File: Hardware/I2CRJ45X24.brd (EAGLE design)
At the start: 216 x 50 mm, 129 parts, among them IC1 MCP23017SO, IC2 MCP23017SO, IC3 MCP23017SO, IC4 MCP23017SO, IC5 MCP23017SO, IC6 MCP23017SO, J1 I2C-BREAKOUT, J2 I2C-BREAKOUT, J3 M01-PLAIN, J4 RJ45-X8, J5 RJ45-X8, J6 RJ45-X8

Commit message: Major rework for v3.0 release of all versions.
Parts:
- R101: value 22K -> 10K
- SJ3: device SuperHouse-Jumpers:SJC -> SuperHouse-Jumpers:SJ
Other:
- board text added: "24-Port I2C RJ45 Breakout"
- board text removed: "24-Channel I2C RJ45 Breakout"
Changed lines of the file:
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@@
 </layers>
 <board>
-<fusionsync huburn="a.cGVyc29uYWw6dWUyZDliZmNi" projecturn="a.cGVyc29uYWw6dWUyZDliZmNiIzIwMTkwNjE5MTk5NjgzNjgx" f3durn="urn:adsk.wipprod:dm.lineage:7PE12rU6Rs2d8xNWJ3I8mw" pcbguid="240f1cde-c83f-4e3e-9fac-562d2bf45fdf" lastpulledtime="" lastsyncedchangeguid="1491f9b9-a179-9c0a-9821-19275fe4b9b0" latestrevisionid="" lastsyncedrevisionid="" lastboardhashguid="57911f44-b240-5674-ec1f-8acbffdfcb08" lastpushedtime="2021-04-15T04:03:47Z" linktopcb3d="false"/>
+<fusionsync huburn="a.cGVyc29uYWw6dWUyZDliZmNi" projecturn="a.cGVyc29uYWw6dWUyZDliZmNiIzIwMTkwNjE5MTk5NjgzNjgx" f3durn="urn:adsk.wipprod:dm.lineage:7PE12rU6Rs2d8xNWJ3I8mw" pcbguid="240f1cde-c83f-4e3e-9fac-562d2bf45fdf" lastpulledtime="" lastsyncedchangeguid="1491f9b9-a179-9c0a-9821-19275fe4b9b0" latestrevisionid="" lastsyncedrevisionid="" lastboardhashguid="93750741-3b2d-7ddd-64bd-c7f7c55b0702" lastpushedtime="2021-04-15T05:51:18Z" linktopcb3d="false"/>
 <plain>
 <wire x1="3" y1="0" x2="0" y2="3" width="0" layer="20" curve="-90"/>
@@
 <text x="50.045" y="43.854" size="3.1" layer="22" font="vector" ratio="17" distance="30" rot="MR0" align="center-left">Super
 House</text>
-<text x="60.045" y="27" size="2.8" layer="22" font="vector" ratio="17" distance="20" rot="MR0">24-Channel
+<text x="60.045" y="27" size="2.8" layer="22" font="vector" ratio="17" distance="20" rot="MR0">24-Port
 I2C RJ45
 Breakout</text>
@@
 <text x="4.5" y="12" size="1.6" layer="21" font="vector" ratio="17" distance="20" align="bottom-center">Super
 House</text>
-<text x="12" y="47.354" size="1.8" layer="21" font="vector" ratio="17" distance="30">24-Channel I2C RJ45 Breakout</text>
+<text x="11" y="47.354" size="2.1844" layer="21" font="vector" ratio="17" distance="30">24-Port I2C RJ45 Breakout</text>
 <text x="32" y="45.354" size="1.6764" layer="21" font="vector" ratio="17" distance="30">by Jon Oxer</text>
 <text x="40.5" y="24.955" size="1.9304" layer="21" font="vector" ratio="17" rot="R90">VCC: 1.8-5.5V
@@
 <attribute name="VALUE" x="122.484" y="46.603" size="0.4064" layer="27"/>
 </element>
-<element name="SJ2" library="SuperHouse-Jumpers" library_urn="urn:adsk.eagle:library:12190622" package="SJ" package3d_urn="urn:adsk.eagle:package:7066338/1" value="SCL PU" x="64.5" y="46" smashed="yes" rot="R90">
+<element name="SJ2" library="SuperHouse-Jumpers" library_urn="urn:adsk.eagle:library:12190622" package="SJ" package3d_urn="urn:adsk.eagle:package:7066338/2" value="SCL PU" x="64.5" y="46" smashed="yes" rot="R90">
 <attribute name="NAME" x="63.357" y="44.349" size="1.27" layer="25" ratio="10" rot="R90"/>
 <attribute name="VALUE" x="64.5" y="46.4001" size="0.02" layer="27" rot="R90"/>
 </element>
-<element name="SJ1" library="SuperHouse-Jumpers" library_urn="urn:adsk.eagle:library:12190622" package="SJ" package3d_urn="urn:adsk.eagle:package:7066338/1" value="SDA PU" x="61.5" y="46" smashed="yes" rot="R90">
+<element name="SJ1" library="SuperHouse-Jumpers" library_urn="urn:adsk.eagle:library:12190622" package="SJ" package3d_urn="urn:adsk.eagle:package:7066338/2" value="SDA PU" x="61.5" y="46" smashed="yes" rot="R90">
 <attribute name="NAME" x="60.357" y="44.349" size="1.27" layer="25" ratio="10" rot="R90"/>
 <attribute name="VALUE" x="61.5" y="46.4001" size="0.02" layer="27" rot="R90"/>
@@
 <attribute name="VALUE" x="214.9652" y="20.984" size="0.4064" layer="27" font="vector" rot="R90"/>
 </element>
-<element name="R101" library="SuperHouse-DiscreteSemi" library_urn="urn:adsk.eagle:library:11768461" package="R0603" package3d_urn="urn:adsk.eagle:package:11768543/2" value="22K" x="3.6" y="23.1" smashed="yes" rot="R180">
+<element name="R101" library="SuperHouse-DiscreteSemi" library_urn="urn:adsk.eagle:library:11768461" package="R0603" package3d_urn="urn:adsk.eagle:package:11768543/2" value="10K" x="3.6" y="23.1" smashed="yes" rot="R180">
 <attribute name="NAME" x="4.489" y="22.592" size="0.4064" layer="25" font="vector" rot="R180"/>
 <attribute name="VALUE" x="4.616" y="24.0652" size="0.4064" layer="27" font="vector" rot="R180"/>
 </element>
-<element name="SJ3" library="SuperHouse-Jumpers" library_urn="urn:adsk.eagle:library:12190622" package="SJC" package3d_urn="urn:adsk.eagle:package:7066342/2" value="RST-PU" x="8.4" y="46.9" smashed="yes" rot="R270">
+<element name="SJ3" library="SuperHouse-Jumpers" library_urn="urn:adsk.eagle:library:12190622" package="SJ" package3d_urn="urn:adsk.eagle:package:7066338/2" value="RST-PU" x="8.4" y="46.9" smashed="yes" rot="R270">
 <attribute name="NAME" x="9.543" y="48.551" size="1.27" layer="25" ratio="10" rot="R270"/>
 <attribute name="VALUE" x="8.4" y="46.4999" size="0.02" layer="27" rot="R270"/>
@@
 <wire x1="115.62" y1="42.62" x2="115" y2="42" width="0.4064" layer="1"/>
 <wire x1="83" y1="42" x2="82.9" y2="41.9" width="0.3048" layer="1"/>
-<wire x1="82.9" y1="41.9" x2="70" y2="41.9" width="0.3048" layer="1"/>
-<wire x1="70" y1="41.9" x2="62.9" y2="41.9" width="0.3048" layer="1"/>
-<wire x1="62.9" y1="41.9" x2="62" y2="41" width="0.3048" layer="1"/>
-<wire x1="62" y1="41" x2="62" y2="40" width="0.3048" layer="1"/>
-<wire x1="62" y1="40" x2="59.54" y2="37.54" width="0.3048" layer="1"/>
-<wire x1="59.54" y1="37.54" x2="58.78" y2="37.54" width="0.3048" layer="1"/>
+<wire x1="82.9" y1="41.9" x2="70" y2="41.9" width="0.4064" layer="1"/>
+<wire x1="70" y1="41.9" x2="62.9" y2="41.9" width="0.4064" layer="1"/>
+<wire x1="62.9" y1="41.9" x2="62" y2="41" width="0.4064" layer="1"/>
+<wire x1="62" y1="41" x2="62" y2="40" width="0.4064" layer="1"/>
+<wire x1="62" y1="40" x2="59.54" y2="37.54" width="0.4064" layer="1"/>
+<wire x1="59.54" y1="37.54" x2="58.78" y2="37.54" width="0.4064" layer="1"/>
 <wire x1="64.5" y1="46.762" x2="61.5" y2="46.762" width="0.3048" layer="1"/>
 <wire x1="61.5" y1="46.762" x2="60.238" y2="46.762" width="0.3048" layer="1"/>

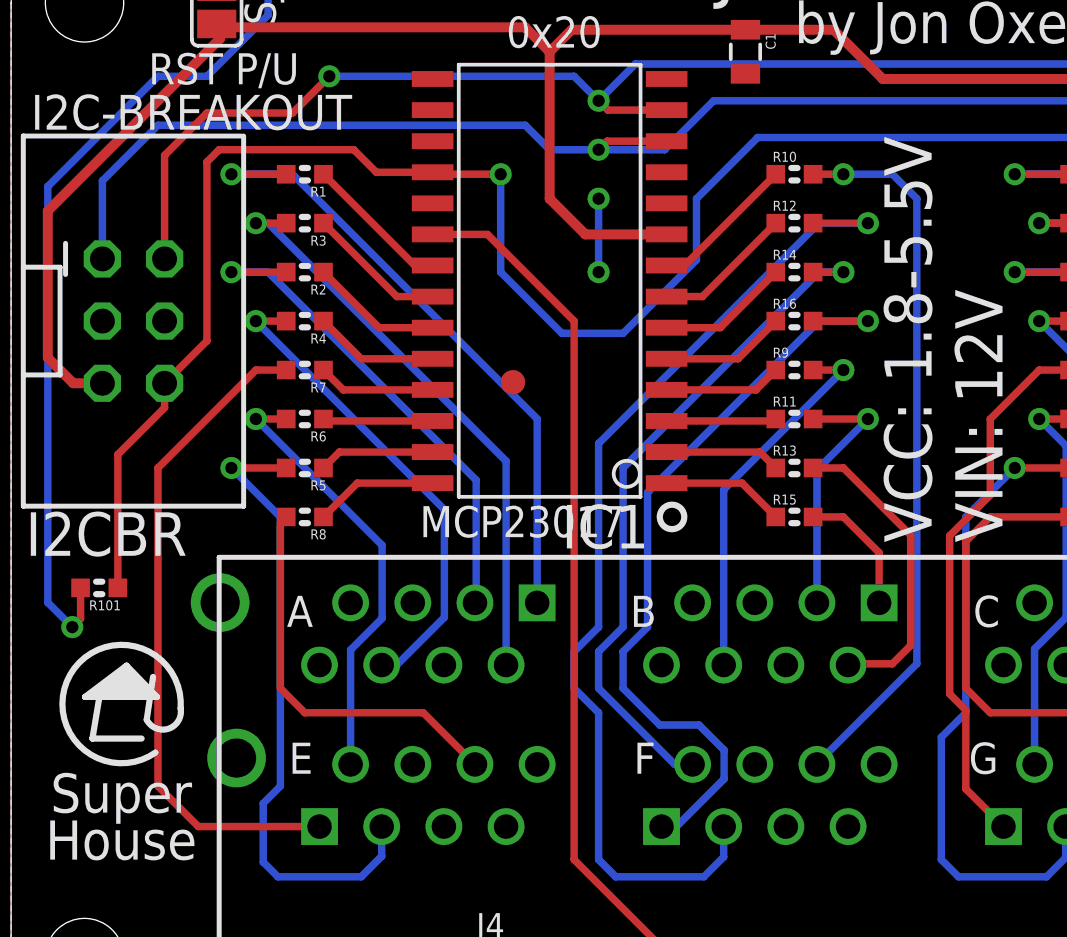
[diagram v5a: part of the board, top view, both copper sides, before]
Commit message: Began replacement of discrete resistors with resistor arrays.
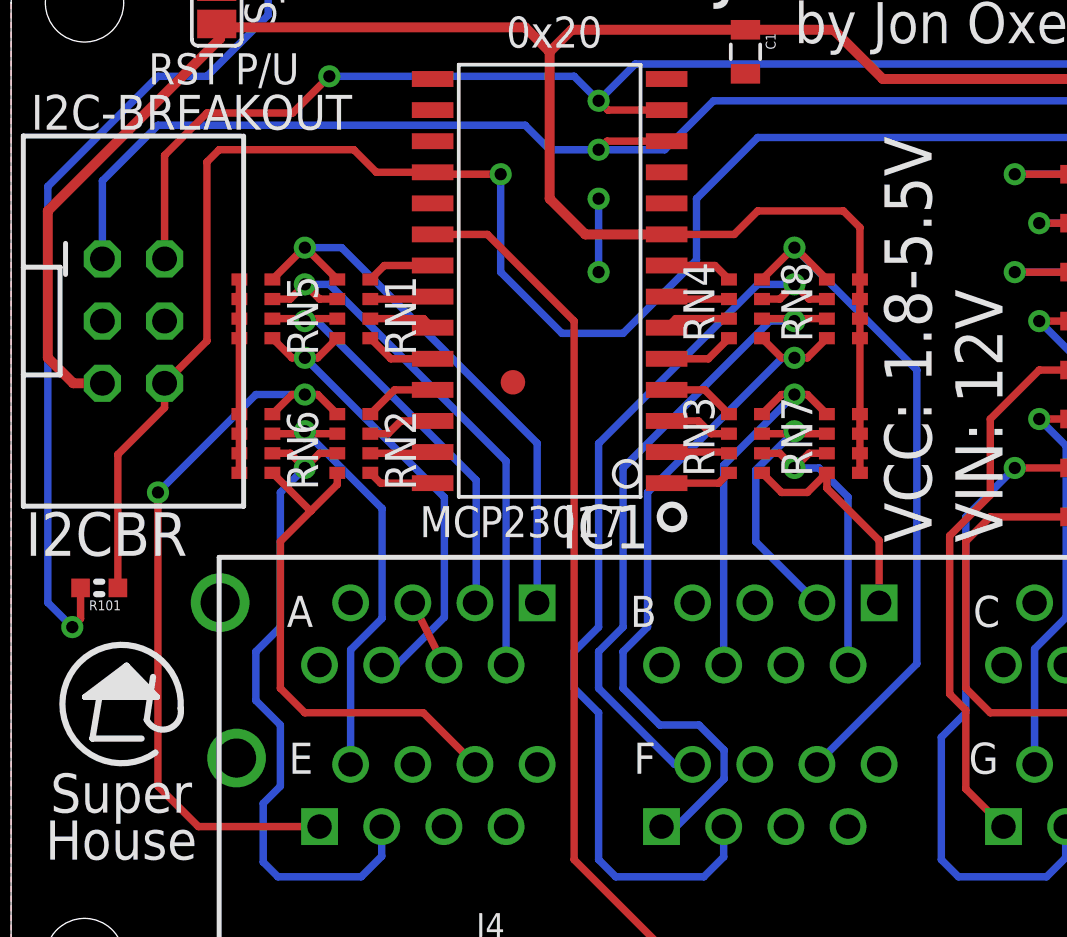
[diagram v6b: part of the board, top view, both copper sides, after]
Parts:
- removed R1, R10, R11, R12, R13, R14, R15, R16, R2, R3, R4, R5, R6, R7, R8, R9: 1K, SuperHouse-DiscreteSemi:R0603
- added RN1, RN2, RN3, RN4: 1K, SuperHouse-DiscreteSemi:CAY16
- added RN5, RN6, RN7, RN8: (no value), SuperHouse-DiscreteSemi:CAY16
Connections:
- net 1A1: now also RN1.5, RN5.4; no longer R1.2
- net 1A2: now also RN1.6, RN5.3; no longer R3.2
- net 1A3: now also RN1.7, RN5.2; no longer R2.2
- net 1A6: now also RN1.8, RN5.1; no longer R4.2
- net 1B1: now also RN3.5, RN7.4; no longer R15.2
- net 1B2: now also RN3.6, RN7.3; no longer R13.2
- net 1B3: now also RN3.7, RN7.2; no longer R11.2
- net 1B6: now also RN3.8, RN7.1; no longer R9.2
- net 1E1: now also RN2.5, RN6.4; no longer R7.2
- net 1E2: now also RN2.6, RN6.3; no longer R6.2
- net 1E3: now also RN2.7, RN6.2; no longer R5.2
- net 1E6: now also RN2.8, RN6.1; no longer R8.2
- net 1F1: now also RN4.5, RN8.4; no longer R16.2
- net 1F2: now also RN4.6, RN8.3; no longer R14.2
- net 1F3: now also RN4.7, RN8.2; no longer R12.2
- net 1F6: now also RN4.8, RN8.1; no longer R10.2
- net GPA0-1: now also RN1.4; no longer R1.1
- net GPA1-1: now also RN1.3; no longer R3.1
- net GPA2-1: now also RN1.2; no longer R2.1
- net GPA3-1: now also RN1.1; no longer R4.1
- net GPA4-1: now also RN2.4; no longer R7.1
- net GPA5-1: now also RN2.3; no longer R6.1
- net GPA6-1: now also RN2.2; no longer R5.1
- net GPA7-1: now also RN2.1; no longer R8.1
- net GPB0-1: now also RN3.4; no longer R15.1
- net GPB1-1: now also RN3.3; no longer R13.1
- net GPB2-1: now also RN3.2; no longer R11.1
- net GPB3-1: now also RN3.1; no longer R9.1
- net GPB4-1: now also RN4.4; no longer R16.1
- net GPB5-1: now also RN4.3; no longer R14.1
- net GPB6-1: now also RN4.2; no longer R12.1
- net GPB7-1: now also RN4.1; no longer R10.1
- net VCC: now also RN5.5, RN5.6, RN5.7, RN5.8, RN6.5, RN6.6, RN6.7, RN6.8, RN7.5, RN7.6, RN7.7, RN7.8, RN8.5, RN8.6, RN8.7, RN8.8
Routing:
- net VCC: track 327.1 -> 353.6 mm
- net 1E6: track 16.3 -> 21.2 mm
- net 1B1: track 5.35 -> 9.51 mm
- net 1A1: track 26.4 -> 23.0 mm
- net 1A3: track 20.8 -> 17.5 mm
- net GPB7-1: track 6.00 -> 2.78 mm
- net GPA0-1: track 6.00 -> 2.78 mm
- net 1F3: track 41.8 -> 38.6 mm
- net GPB6-1: track 5.70 -> 2.59 mm
- net GPA1-1: track 5.70 -> 2.59 mm
- net 1E1: track 27.2 -> 30.3 mm, vias 0 -> 2
- net VIN: track 16.7 -> 19.6 mm
- net GPB5-1: track 5.40 -> 2.70 mm
- net GPA2-1: track 5.40 -> 2.70 mm
- net 1F1: track 32.3 -> 29.7 mm
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
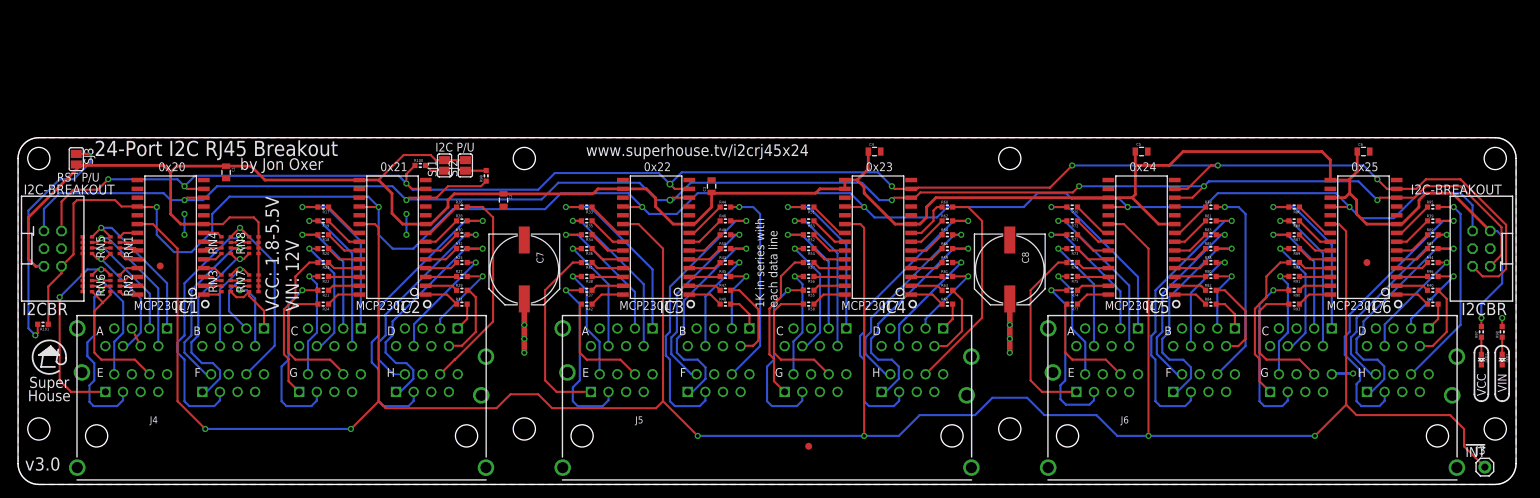
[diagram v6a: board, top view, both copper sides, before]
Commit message: Progress on converting resistors to arrays and adding pullups.
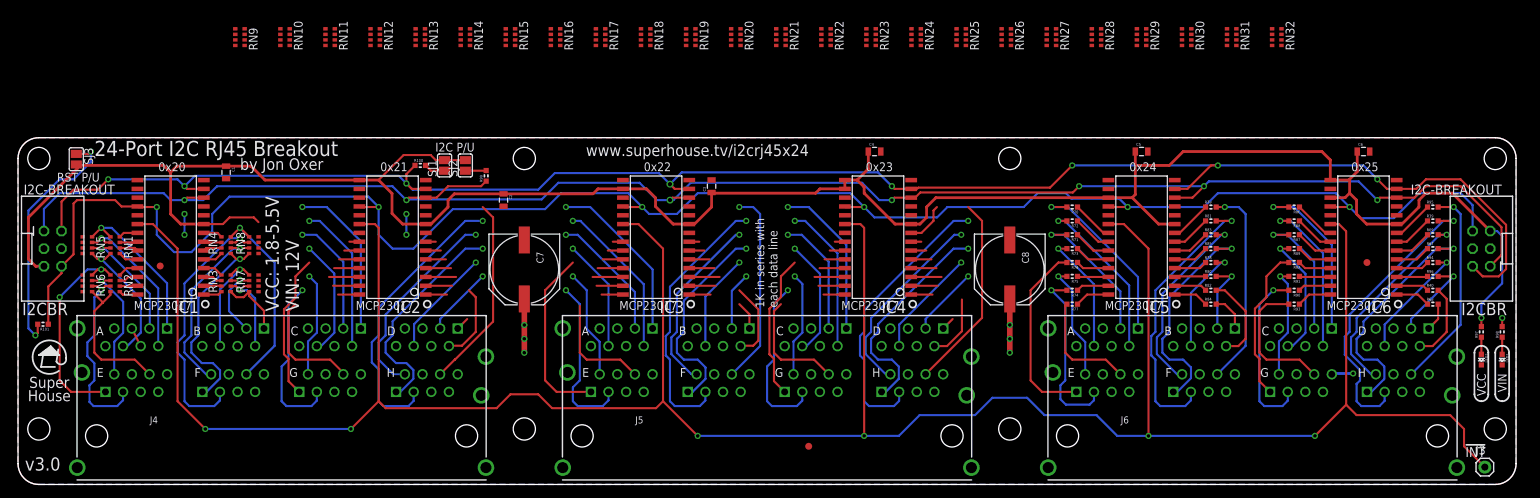
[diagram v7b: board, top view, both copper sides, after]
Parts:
- removed R17, R18, R19, R20, R21, R22, R23, R24, R25, R26, R27, R28, R29, R30, R31, R32, R33, R34, R35, R36, R37, R38, R41, R42, R43, R44, R45, R46, R47, R48, R49, R50, R51, R52, R53, R54, R55, R56, R57, R58, R59, R60, R61, R62, R63, R64, R65, R66: 1K, SuperHouse-DiscreteSemi:R0603
- added RN10, RN11, RN12, RN17, RN18, RN19, RN20, RN25, RN26, RN27, RN28, RN9: 1K, SuperHouse-DiscreteSemi:CAY16
- added RN13, RN14, RN15, RN16, RN21, RN22, RN23, RN24, RN29, RN30, RN31, RN32: 10K, SuperHouse-DiscreteSemi:CAY16
- RN5, RN6, RN7, RN8: value (none) -> 10K
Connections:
- net 1C1: now also RN13.4, RN9.5; no longer R17.2
- net 1C2: now also RN13.3, RN9.6; no longer R19.2
- net 1C3: now also RN13.2, RN9.7; no longer R18.2
- net 1C6: now also RN13.1, RN9.8; no longer R20.2
- net 1D1: now also RN11.5, RN15.4; no longer R31.2
- net 1D2: now also RN11.6, RN15.3; no longer R29.2
- net 1D3: now also RN11.7, RN15.2; no longer R27.2
- net 1D6: now also RN11.8, RN15.1; no longer R25.2
- net 1G1: now also RN10.5, RN14.4; no longer R23.2
- net 1G2: now also RN10.6, RN14.3; no longer R22.2
- net 1G3: now also RN10.7, RN14.2; no longer R21.2
- net 1G6: now also RN10.8, RN14.1; no longer R24.2
- net 1H1: now also RN12.5, RN16.4; no longer R32.2
- net 1H2: now also RN12.6, RN16.3; no longer R30.2
- net 1H3: now also RN12.7, RN16.2; no longer R28.2
- net 1H6: now also RN12.8, RN16.1; no longer R26.2
- net 2A1: now also RN17.5, RN21.4; no longer R33.2
- net 2A2: now also RN17.6, RN21.3; no longer R35.2
- net 2A3: now also RN17.7, RN21.2; no longer R34.2
- net 2A6: now also RN17.8, RN21.1; no longer R36.2
- net 2B1: now also RN19.5, RN23.4; no longer R49.2
- net 2B2: now also RN19.6, RN23.3; no longer R47.2
- net 2B3: now also RN19.7, RN23.2; no longer R45.2
- net 2B6: now also RN19.8, RN23.1; no longer R43.2
- net 2C1: now also RN25.5, RN29.4; no longer R51.2
- net 2C2: now also RN25.6, RN29.3; no longer R53.2
- net 2C3: now also RN25.7, RN29.2; no longer R52.2
- net 2C6: now also RN25.8, RN29.1; no longer R54.2
- net 2D1: now also RN27.5, RN31.4; no longer R65.2
- net 2D2: now also RN27.6, RN31.3; no longer R63.2
- net 2D3: now also RN27.7, RN31.2; no longer R61.2
- net 2D6: now also RN27.8, RN31.1; no longer R59.2
- net 2E1: now also RN18.5, RN22.4; no longer R41.2
- net 2E2: now also RN18.6, RN22.3; no longer R38.2
- net 2E3: now also RN18.7, RN22.2; no longer R37.2
- net 2E6: now also RN18.8, RN22.1; no longer R42.2
- net 2F1: now also RN20.5, RN24.4; no longer R50.2
- net 2F2: now also RN20.6, RN24.3; no longer R48.2
- net 2F3: now also RN20.7, RN24.2; no longer R46.2
- net 2F6: now also RN20.8, RN24.1; no longer R44.2
- net 2G1: now also RN26.5, RN30.4; no longer R57.2
- net 2G2: now also RN26.6, RN30.3; no longer R56.2
- net 2G3: now also RN26.7, RN30.2; no longer R55.2
- net 2G6: now also RN26.8, RN30.1; no longer R58.2
- net 2H1: now also RN28.5, RN32.4; no longer R66.2
- net 2H2: now also RN28.6, RN32.3; no longer R64.2
- net 2H3: now also RN28.7, RN32.2; no longer R62.2
- net 2H6: now also RN28.8, RN32.1; no longer R60.2
- net GPA0-2: now also RN9.4; no longer R17.1
- net GPA0-3: now also RN17.4; no longer R33.1
- net GPA0-4: now also RN25.4; no longer R51.1
- net GPA1-2: now also RN9.3; no longer R19.1
- net GPA1-3: now also RN17.3; no longer R35.1
- net GPA1-4: now also RN25.3; no longer R53.1
- net GPA2-2: now also RN9.2; no longer R18.1
- net GPA2-3: now also RN17.2; no longer R34.1
- net GPA2-4: now also RN25.2; no longer R52.1
- net GPA3-2: now also RN9.1; no longer R20.1
- net GPA3-3: now also RN17.1; no longer R36.1
- net GPA3-4: now also RN25.1; no longer R54.1
- net GPA4-2: now also RN10.4; no longer R23.1
- net GPA4-3: now also RN18.4; no longer R41.1
- net GPA4-4: now also RN26.4; no longer R57.1
- net GPA5-2: now also RN10.3; no longer R22.1
- net GPA5-3: now also RN18.3; no longer R38.1
- net GPA5-4: now also RN26.3; no longer R56.1
- net GPA6-2: now also RN10.2; no longer R21.1
- net GPA6-3: now also RN18.2; no longer R37.1
- net GPA6-4: now also RN26.2; no longer R55.1
- net GPA7-2: now also RN10.1; no longer R24.1
- net GPA7-3: now also RN18.1; no longer R42.1
- net GPA7-4: now also RN26.1; no longer R58.1
- net GPB0-2: now also RN11.4; no longer R31.1
- net GPB0-3: now also RN19.4; no longer R49.1
- net GPB0-4: now also RN27.4; no longer R65.1
- net GPB1-2: now also RN11.3; no longer R29.1
- net GPB1-3: now also RN19.3; no longer R47.1
- net GPB1-4: now also RN27.3; no longer R63.1
- net GPB2-2: now also RN11.2; no longer R27.1
- net GPB2-3: now also RN19.2; no longer R45.1
- net GPB2-4: now also RN27.2; no longer R61.1
- net GPB3-2: now also RN11.1; no longer R25.1
- net GPB3-3: now also RN19.1; no longer R43.1
- net GPB3-4: now also RN27.1; no longer R59.1
- net GPB4-2: now also RN12.4; no longer R32.1
- net GPB4-3: now also RN20.4; no longer R50.1
- net GPB4-4: now also RN28.4; no longer R66.1
- net GPB5-2: now also RN12.3; no longer R30.1
- net GPB5-3: now also RN20.3; no longer R48.1
- net GPB5-4: now also RN28.3; no longer R64.1
- net GPB6-2: now also RN12.2; no longer R28.1
- net GPB6-3: now also RN20.2; no longer R46.1
- net GPB6-4: now also RN28.2; no longer R62.1
- net GPB7-2: now also RN12.1; no longer R26.1
- net GPB7-3: now also RN20.1; no longer R44.1
- net GPB7-4: now also RN28.1; no longer R60.1
- net VCC: now also RN13.5, RN13.6, RN13.7, RN13.8, RN14.5, RN14.6, RN14.7, RN14.8, RN15.5, RN15.6, RN15.7, RN15.8, RN16.5, RN16.6, RN16.7, RN16.8, RN21.5, RN21.6, RN21.7, RN21.8, RN22.5, RN22.6, RN22.7, RN22.8, RN23.5, RN23.6, RN23.7, RN23.8, RN24.5, RN24.6, RN24.7, RN24.8, RN29.5, RN29.6, RN29.7, RN29.8, RN30.5, RN30.6, RN30.7, RN30.8, RN31.5, RN31.6, RN31.7, RN31.8, RN32.5, RN32.6, RN32.7, RN32.8
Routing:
- net VCC: track 353.6 -> 335.7 mm
- net GPB7-3: track 6.00 -> 0.73 mm
- net GPA0-4: track 6.00 -> 0.73 mm
- net GPA0-3: track 6.00 -> 0.73 mm
- net GPB7-2: track 6.00 -> 0.73 mm
- net GPA0-2: track 6.00 -> 0.73 mm
- net GPB6-4: track 5.70 -> 1.46 mm
- net GPB6-3: track 5.70 -> 1.46 mm
- net GPB6-2: track 5.70 -> 1.46 mm
- net GPA1-4: track 5.70 -> 1.46 mm
- net GPA1-3: track 5.70 -> 1.46 mm
- net GPA1-2: track 5.70 -> 1.46 mm
- net 2G6: track 19.8 -> 16.6 mm
- net 1G6: track 20.0 -> 16.7 mm
- net GPB5-4: track 5.40 -> 2.19 mm
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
